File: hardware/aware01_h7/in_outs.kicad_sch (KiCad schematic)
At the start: 33 parts, among them J11 InL, J13 OutR, J4 InR, J6 OutL, U10 NE5532DRG4, U9 NE5532DRG4

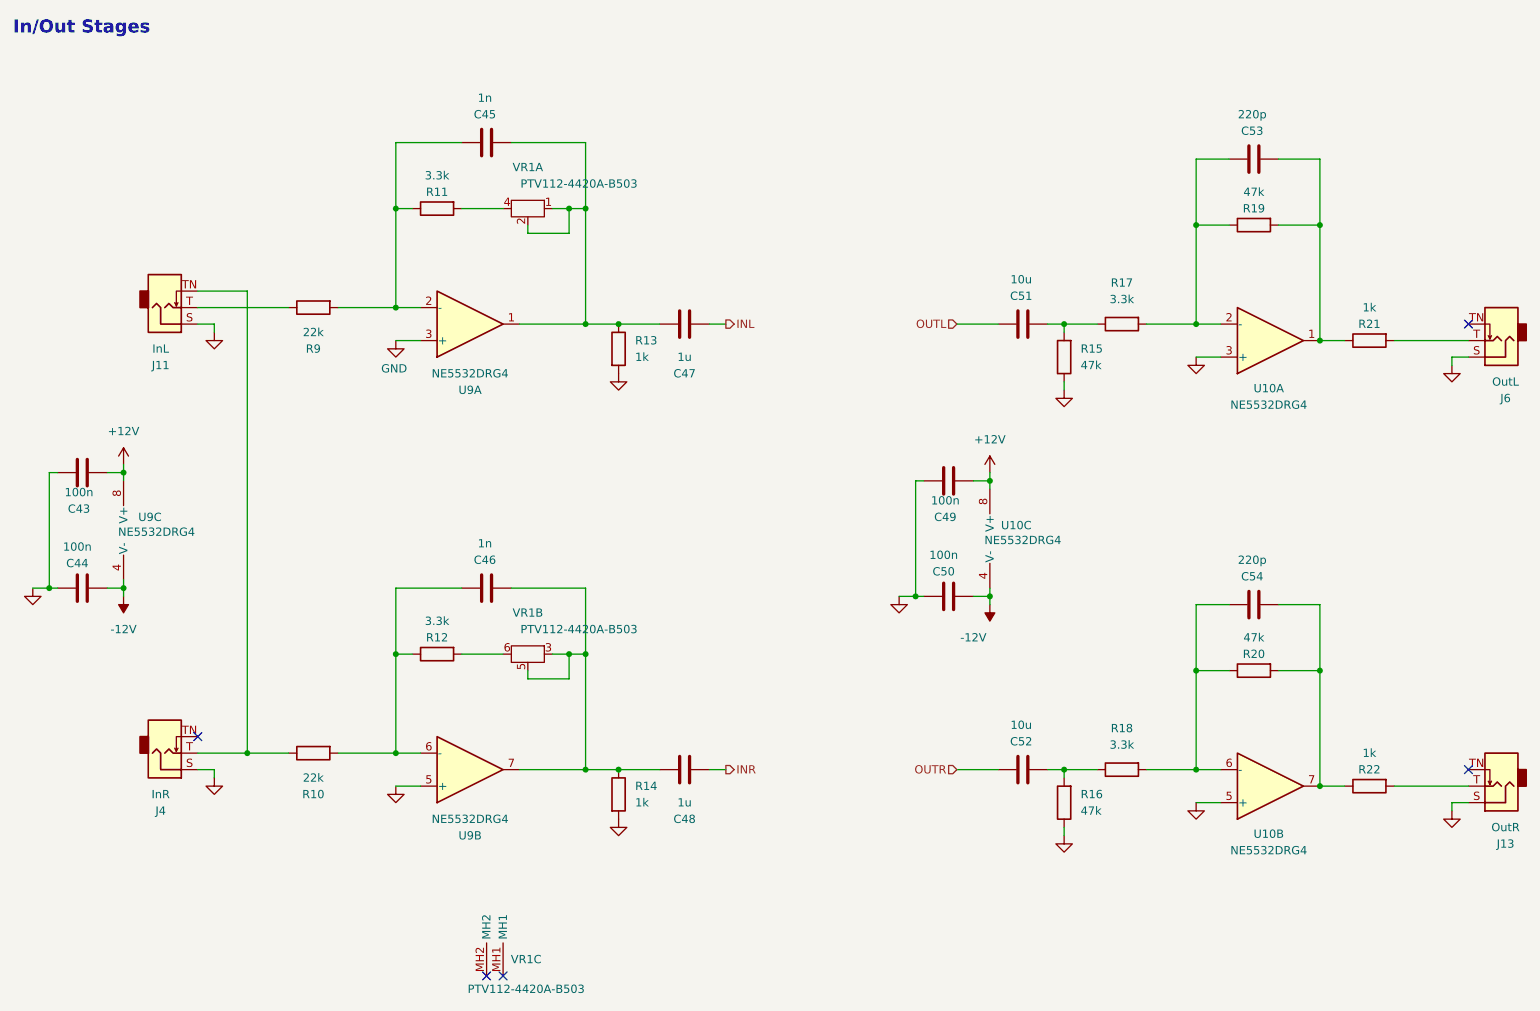
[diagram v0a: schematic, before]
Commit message: rework layout and insert eletrolytic caps for gainstages
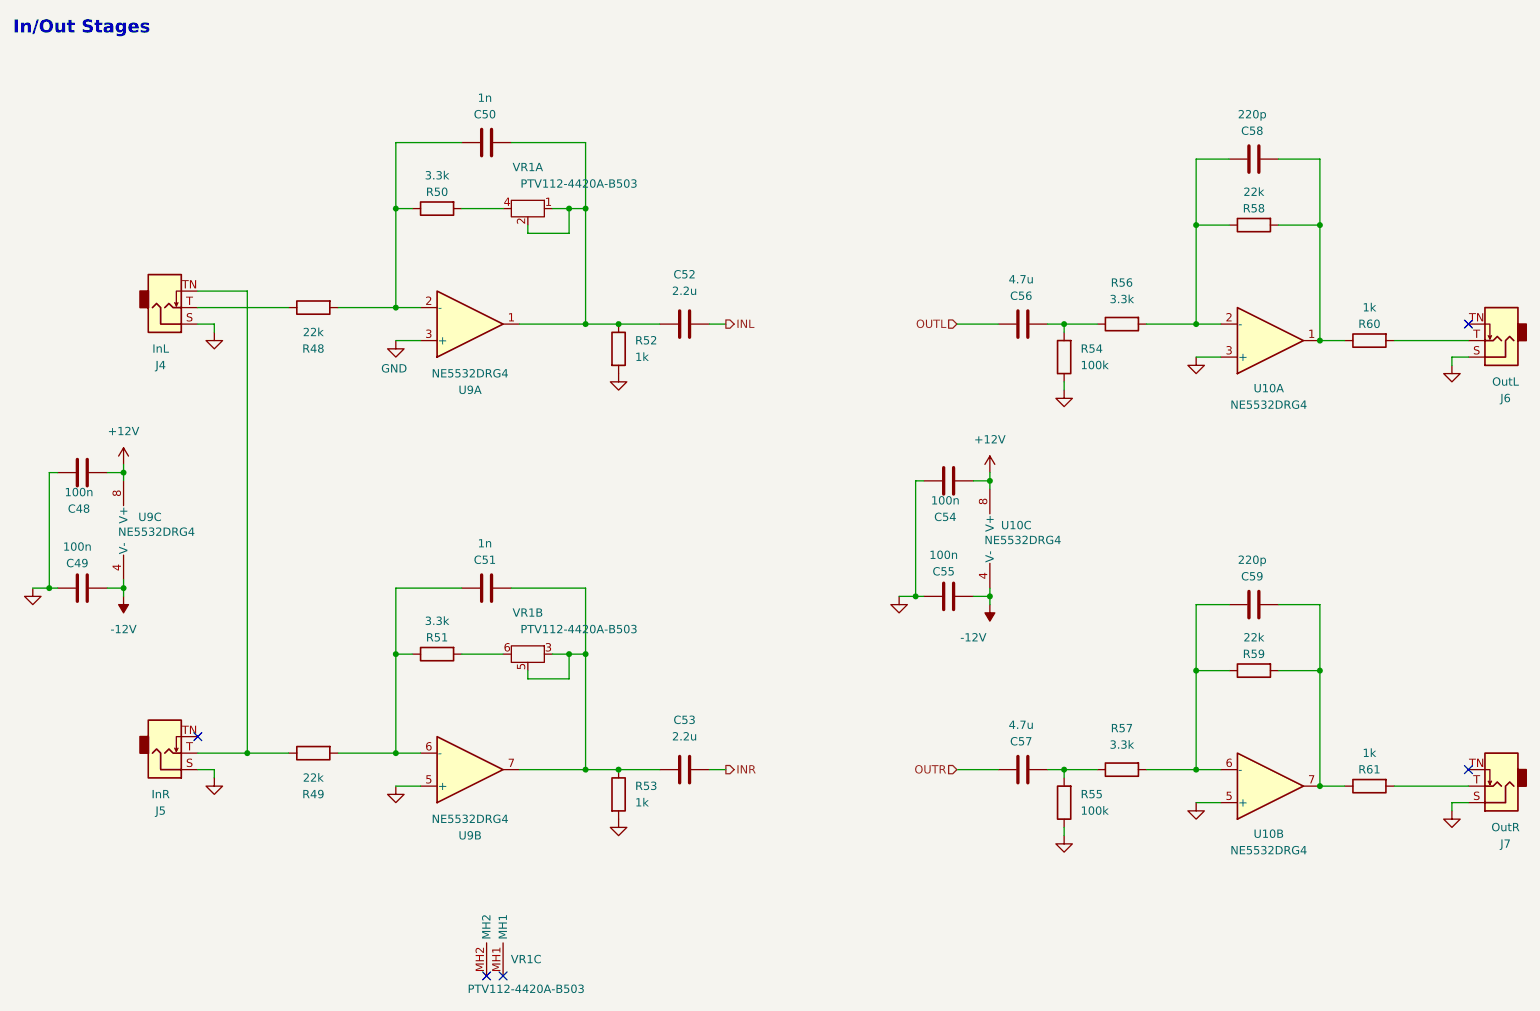
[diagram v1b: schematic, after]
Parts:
- removed C47, C48: 1u, Capacitor_SMD:C_0603_1608Metric, symbol Device:C
- added C53: 2.2u, Capacitor_SMD:CP_Elec_4x5.4, symbol Device:C
- added C57: 4.7u, Capacitor_SMD:CP_Elec_4x5.4, symbol Device:C
- C52: value 10u -> 2.2u; footprint Capacitor_SMD:C_0603_1608Metric -> Capacitor_SMD:CP_Elec_4x5.4; Manufacturer_Name (none) -> Panasonic; Manufacturer_Part_Number (none) -> EEE-1VA2R2NR; Mouser Part Number (none) -> 667-EEE-1VA2R2NR
- C56: renamed from C51; value 10u -> 4.7u; footprint Capacitor_SMD:C_0603_1608Metric -> Capacitor_SMD:CP_Elec_4x5.4; Manufacturer_Name (none) -> Nichicon; Manufacturer_Part_Number (none) -> UWP1C4R7MCL1GB; Mouser Part Number (none) -> 647-UWP1C4R7MCL
- R54: renamed from R15; value 47k -> 100k
- R55: renamed from R16; value 47k -> 100k
- R58: renamed from R19; value 47k -> 22k
- R59: renamed from R20; value 47k -> 22k
- renumbered C43 to C48, C44 to C49, C45 to C50, C46 to C51, C49 to C54, C50 to C55, C53 to C58, C54 to C59, J11 to J4, J4 to J5, J13 to J7, R9 to R48, R10 to R49, R11 to R50, R12 to R51, R13 to R52, R14 to R53, R17 to R56, R18 to R57, R21 to R60, R22 to R61
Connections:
- net INL: now also C52.2
- net INR: now also C53.2
- net OUTR: now also C57.2; no longer C52.2
- net at C50.1, R52.1, U9.1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: now also C52.1
- net at C51.1, R53.1, U9.7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: now also C53.1
- net at R55.2, R57.1: now also C57.1; no longer C52.1

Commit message: add 3rd Gate In and add resistor part No's
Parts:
- R48, R49, R58, R59: Manufacturer_Name (none) -> YAGEO; Manufacturer_Part_Number (none) -> RT0603FRE1322KL; Mouser Part Number (none) -> 603-RT0603FRE1322KL
- R50, R51, R56, R57: Manufacturer_Name (none) -> YAGEO; Manufacturer_Part_Number (none) -> RC0603FR-073K3P; Mouser Part Number (none) -> 603-RC0603FR-073K3P
- R52, R53, R60, R61: Manufacturer_Name (none) -> YAGEO; Manufacturer_Part_Number (none) -> RT0603FRE071KL; Mouser Part Number (none) -> 603-RT0603FRE071KL
- R54, R55: Manufacturer_Name (none) -> YAGEO; Manufacturer_Part_Number (none) -> RT0603FRE07100KL; Mouser Part Number (none) -> 603-RT0603FRE07100KL
